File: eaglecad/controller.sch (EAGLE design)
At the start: 110 parts, among them J1 CORTEX_DEBUG_PTH, J2 U.FL, J3 U.FL, J4 U.FL, J6 TSV991ILT, J7 TSV991ILT, U1 AS5047P, U2 TCAN330, U3 LM3671MF-3.3, U6 STM32F042K6, X1 16MHZ-2.5x2mm

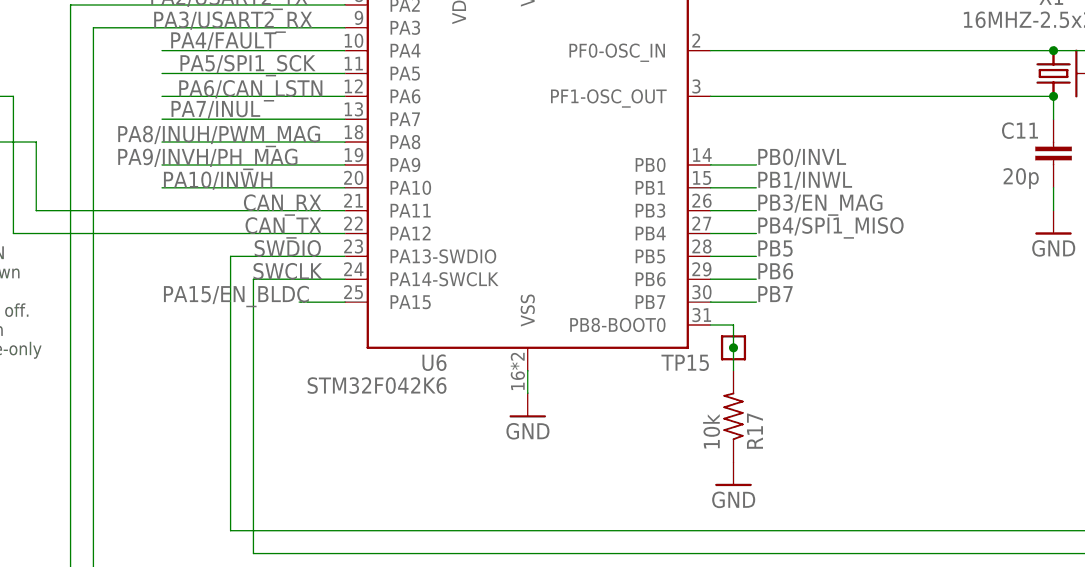
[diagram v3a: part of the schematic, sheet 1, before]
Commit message: Connected the CSn pin of the encoder.
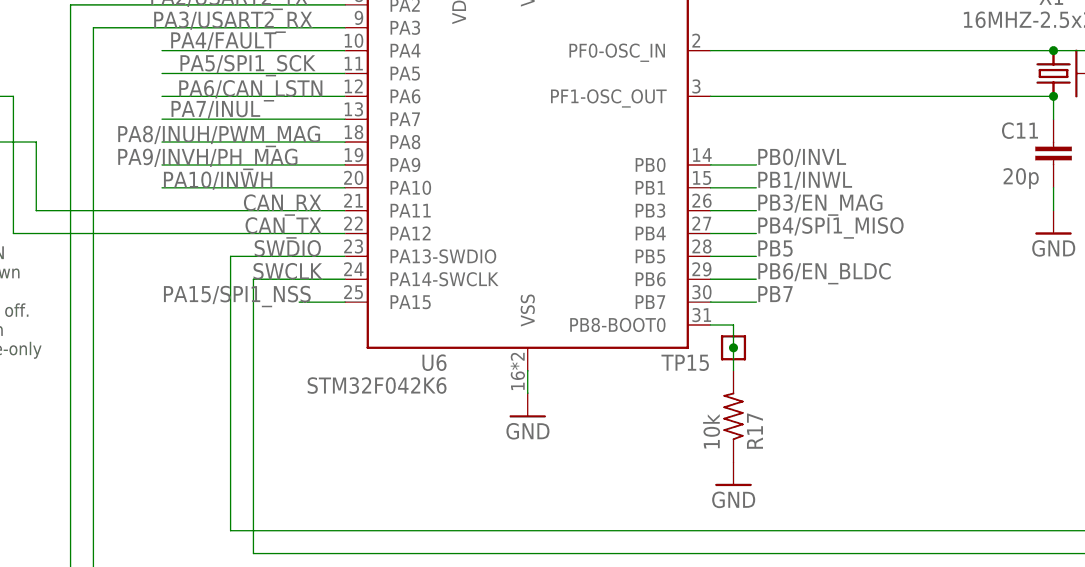
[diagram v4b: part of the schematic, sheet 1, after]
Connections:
- removed net N$9: U1.CSN
- removed net PA15/EN_BLDC: R_EN.2, U6.PA15
- removed net PB6: U6.PB6
- new net PA15/SPI1_NSS: U1.CSN, U6.PA15
- new net PB6/EN_BLDC: R_EN.2, U6.PB6
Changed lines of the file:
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@@
-</segment>
-</net>
-<net name="PA15/EN_BLDC" class="0">
-<segment>
-<pinref part="U6" gate="G$1" pin="PA15"/>
-<wire x1="248.92" y1="114.3" x2="243.84" y2="114.3" width="0.1524" layer="91"/>
-<label x="228.6" y="114.3" size="1.778" layer="95"/>
 </segment>
 </net>
@@
 </segment>
 </net>
-<net name="PB6" class="0">
+<net name="PB6/EN_BLDC" class="0">
 <segment>
 <pinref part="U6" gate="G$1" pin="PB6"/>
@@
 <label x="223.52" y="129.54" size="1.778" layer="95"/>
 <wire x1="248.92" y1="129.54" x2="228.6" y2="129.54" width="0.1524" layer="91"/>
+</segment>
+</net>
+<net name="PA15/SPI1_NSS" class="0">
+<segment>
+<pinref part="U6" gate="G$1" pin="PA15"/>
+<wire x1="248.92" y1="114.3" x2="243.84" y2="114.3" width="0.1524" layer="91"/>
+<label x="228.6" y="114.3" size="1.778" layer="95"/>
 </segment>
 </net>
@@
 </segment>
 </net>
-<net name="PA15/EN_BLDC" class="0">
+<net name="PB6/EN_BLDC" class="0">
 <segment>
 <pinref part="R_EN" gate="G$1" pin="2"/>
@@
 </segment>
 </net>
-<net name="N$9" class="0">
+<net name="PA15/SPI1_NSS" class="0">
 <segment>
 <pinref part="U1" gate="G$1" pin="CSN"/>
 <wire x1="195.58" y1="165.1" x2="185.42" y2="165.1" width="0.1524" layer="91"/>
-</segment>
-</net>
+<label x="172.72" y="165.1" size="1.778" layer="95"/>
+</segment>
+</net>

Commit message: Design review with Nathan. Lots of little changes, mostly cosmetic. Moved from Protocard to smaller ACS board by removing protocard junk.
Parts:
- removed CF1, CF2, CF3: CON-MMCX-F-MOLEX-0734151001, oresat-eagle:CON-MMCX-F-MOLEX-0734151001
- removed CM1: CON-HARTING-FLEX-M-RA-1.27-1515040X601XXX, oresat-eagle:CON-HARTING-FLEX-M-RA-1.27-1515040X601XXX
- removed D3: GREEN, SparkFun-LED:LED-GREEN0603
- removed D4, D5: (no value), adafruit:DIODESMA
- removed J2, J3, J4: U.FL, SparkFun-Connectors:U.FL2PIN
- removed JP2: (no value), pinhead:PINHD-1X12
- removed JP3: (no value), pinhead:PINHD-1X20
- removed JP5, JP6, JP7: (no value), pinhead:PINHD-1X5
- removed R3: 2.7k, rcl_custom:R-US_0402-B-NOSILK
- DRIVER2: device STSPIN250:STSPIN250 -> U-ST-STSPIN250-Brushed-DC-controller:STSPIN250
- JP1: device pinhead:PINHD-2X20 -> pinhead:PINHD-1X4
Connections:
- removed net !SHUTDOWN: CM1.7, CM1.8, JP1.5
- removed net !SHUTDOWN_PH: JP1.6, JP3.3
- removed net CAN_H: CM1.3, CM1.4, JP1.3
- removed net CAN_L: CM1.1, CM1.2, JP1.1
- removed net EN/FAULT: C_EN.1, D4.A, DRIVER1.EN/FAULT, R_EN.1
- removed net N$1: D3.A, R3.1
- removed net N$2: CF2.CENTER, J3.SIGNAL
- removed net N$299: CF1.CENTER, J2.SIGNAL
- removed net N$300: CF3.CENTER, J4.SIGNAL
- removed net SPARE1: CM1.17, CM1.18, JP1.17
- removed net SPARE10: CM1.35, CM1.36, JP1.35
- removed net SPARE10_PH: JP1.36, JP2.10, JP3.18
- removed net SPARE11: CM1.37, CM1.38, JP1.37
- removed net SPARE11_PH: JP1.38, JP2.11, JP3.19
- removed net SPARE12: CM1.39, CM1.40, JP1.39
- removed net SPARE12_PH: JP1.40, JP2.12, JP3.20
- removed net SPARE1_PH: JP1.18, JP2.1, JP3.9
- removed net SPARE2: CM1.19, CM1.20, JP1.19
- removed net SPARE2_PH: JP1.20, JP2.2, JP3.10
- removed net SPARE3: CM1.21, CM1.22, JP1.21
- removed net SPARE3_PH: JP1.22, JP2.3, JP3.11
- removed net SPARE4: CM1.23, CM1.24, JP1.23
- removed net SPARE4_PH: JP1.24, JP2.4, JP3.12
- removed net SPARE5: CM1.25, CM1.26, JP1.25
- removed net SPARE5_PH: JP1.26, JP2.5, JP3.13
- removed net SPARE6: CM1.27, CM1.28, JP1.27
- removed net SPARE6_PH: JP1.28, JP2.6, JP3.14
- removed net SPARE7: CM1.29, CM1.30, JP1.29
- removed net SPARE7_PH: JP1.30, JP2.7, JP3.15
- removed net SPARE8: CM1.31, CM1.32, JP1.31
- removed net SPARE8_PH: JP1.32, JP2.8, JP3.16
- removed net SPARE9: CM1.33, CM1.34, JP1.33
- removed net SPARE9_PH: JP1.34, JP2.9, JP3.17
- removed net VBATT: CM1.13, CM1.14, CM1.15, CM1.16, JP1.7, JP1.9
- net 3.3V: no longer JP3.4, JP5.1, JP5.2, JP5.3, JP5.4, JP5.5, JP6.1, JP6.2, JP6.3, JP6.4, JP6.5
- net CANH_PH: now also JP1.2; no longer JP1.4, JP3.2
- net CAN_L_PH: now also JP1.1; no longer JP1.2, JP3.1
- net FAULT_MAG: no longer D5.A
- net GND: now also JP1.4; no longer CF1.SHIELD, CF2.SHIELD, CF3.SHIELD, CM1.10, CM1.11, CM1.12, CM1.5, CM1.6, CM1.9, D3.C, J2.GND, J3.GND, J4.GND, JP1.12, JP1.14, JP1.16, JP3.6, JP3.7, JP3.8
- net PA0/CURR_FDB_BLDC: no longer R3.2
- net PA4/FAULT: now also C_EN.1, DRIVER1.EN/FAULT, R_EN.1; no longer D4.C, D5.C
- net V_BATT: now also JP1.3; no longer JP1.10, JP1.8, JP3.5, JP7.1, JP7.2, JP7.3, JP7.4, JP7.5
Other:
- note added: "ADD RESISTOR!"
- note added: "BYPASS CAP"
- note added: "CONNECTOR TO ORESAT CARD"
- note added: "FIXME"
- note removed: "What do we connect the CSn pin to? This is for SPI chip select."
- moved on the sheet: C11, C16, C17, C19, C20, C21, C22, C23, C24, C3, C9, D1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

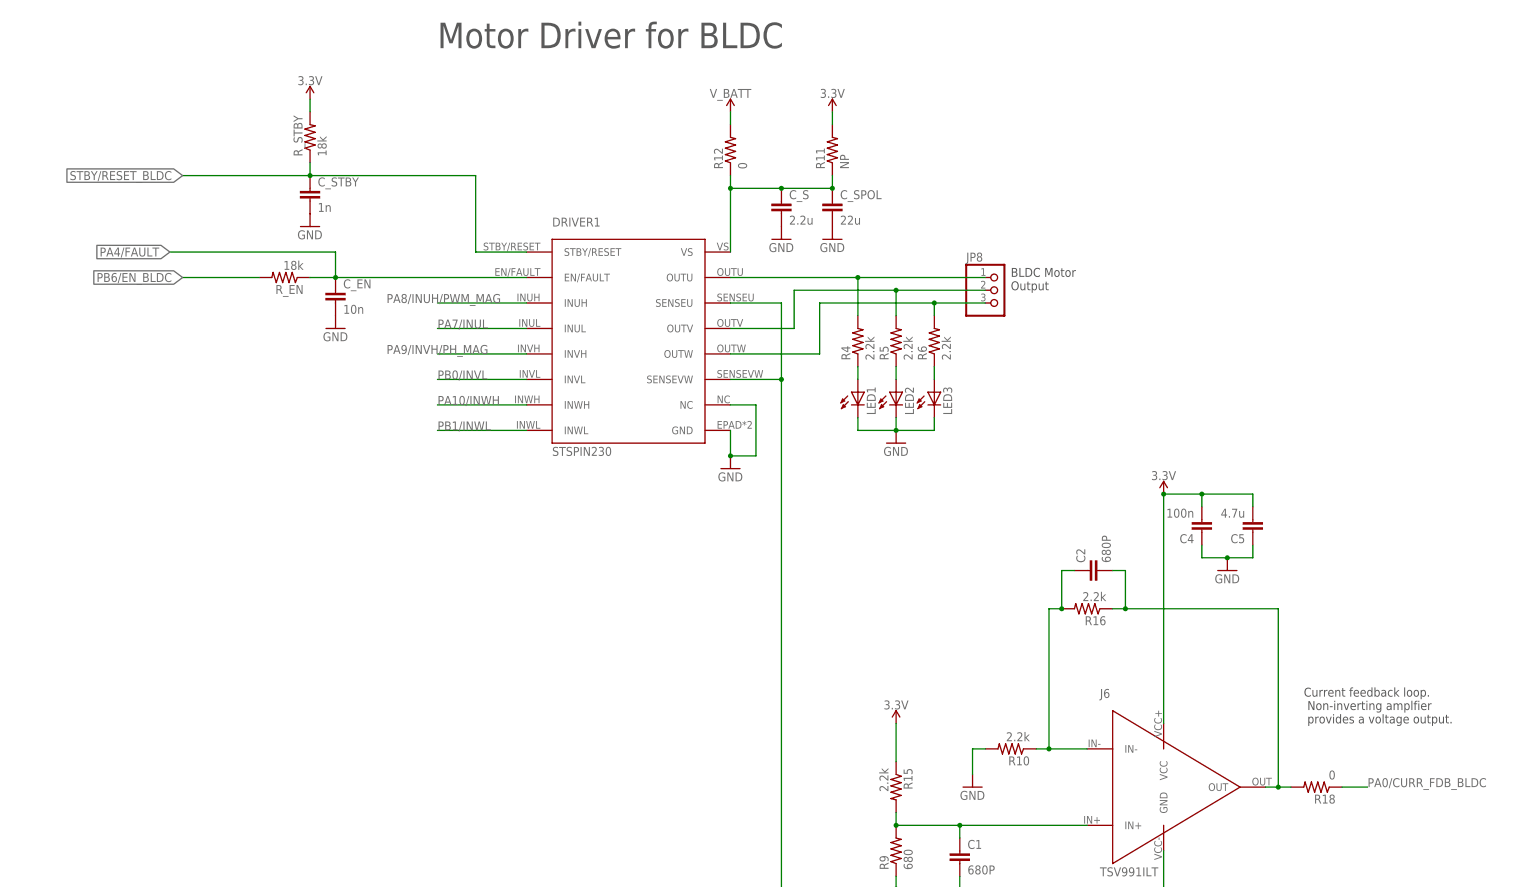
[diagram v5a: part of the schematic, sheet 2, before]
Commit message: Cosmetic fixes: Added labels. All resistors and capacitors are numbered. Updated the symbol of the encoder. Updated the symbol and package of the STSPIN230. Boxed LEDs and placed a note "NP FOR FLIGHT". Other small fixes...
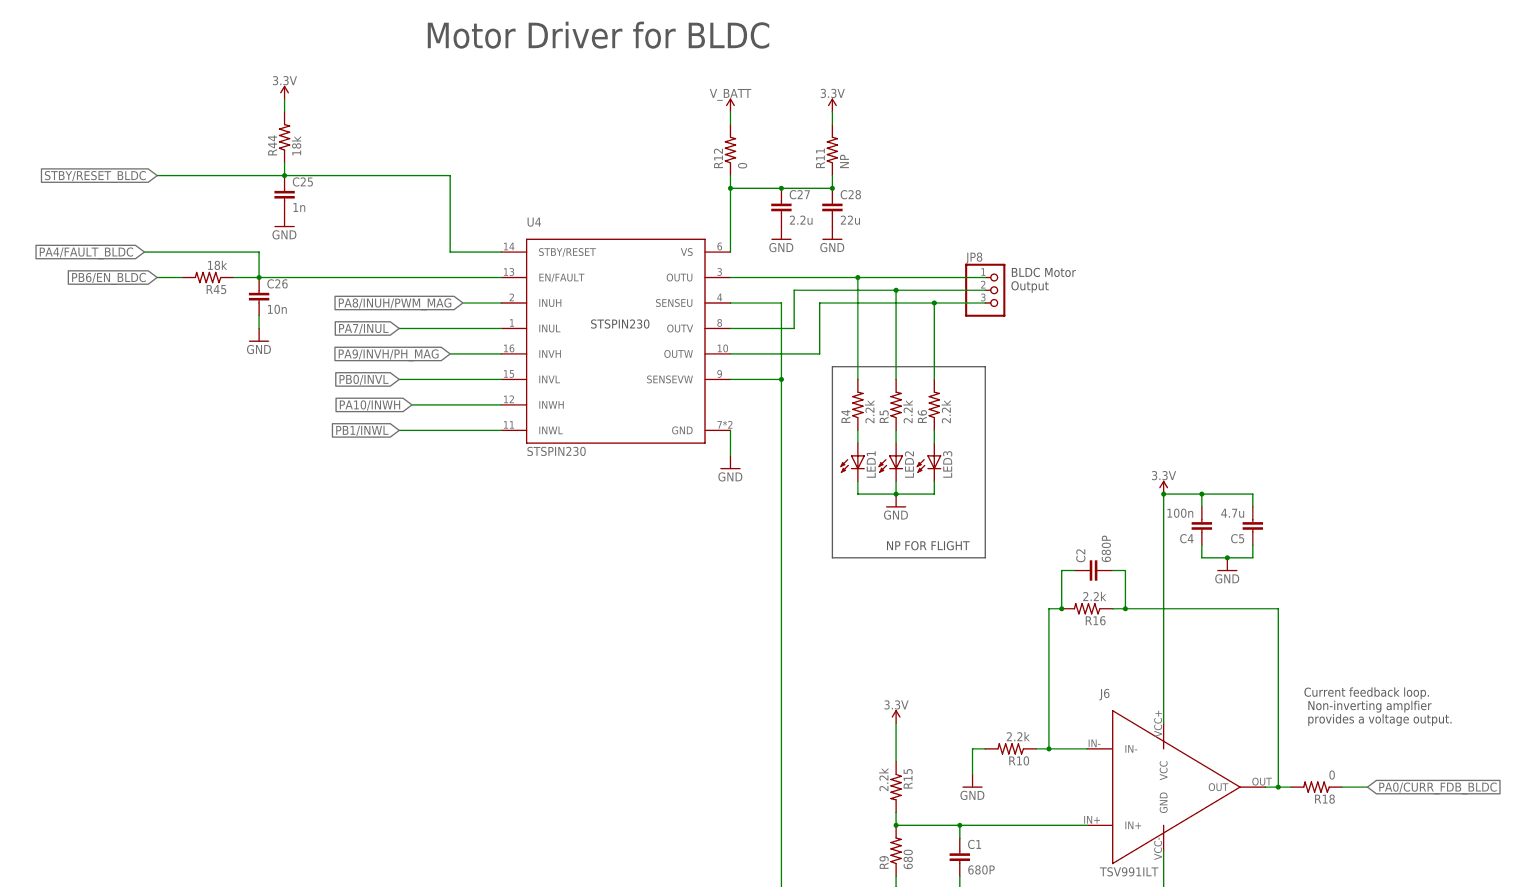
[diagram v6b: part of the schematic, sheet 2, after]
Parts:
- removed C_EN: 10n, rcl:C-EUC0402
- removed C_STBY: 1n, rcl:C-EUC0402
- removed DRIVER1: STSPIN230, STSPIN230:STSPIN230
- removed R_EN, R_STBY: 18k, rcl:R-US_R0402
- added C25: 1n, rcl:C-EUC0402
- added C26: 10n, rcl:C-EUC0402
- added C33: 2.2n, rcl:C-EUC0402
- added R3: 10k, rcl:R-US_R0402
- added R44, R45: 18k, rcl:R-US_R0402
- added U4: STSPIN230, U-ST-STSPIN230-BLDC-controller:STSPIN230
- C6: value 2.2n -> 100n
- U1: device AS5047P:AS5047P -> U-AMS-AS5047P-encoder:AS5047P
- renumbered C_EN1 to C30, C_OFF to C34, C_S to C27, C_S1 to C31, C_SPOL to C28, C_SPOL1 to C32, C_STBY1 to C29, RC_OFF to R48, R_EN1 to R47, R_OFF to R49, R_STBY1 to R46
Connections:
- removed net FAULT_MAG: C30.1, DRIVER2.EN/FAULT, R47.1
- removed net N$21: DRIVER1.OUTW, JP8.3, R6.2
- removed net N$7: DRIVER1.OUTU, JP8.1, R4.2
- removed net N$8: DRIVER1.OUTV, JP8.2, R5.2
- removed net PA4/FAULT: C_EN.1, DRIVER1.EN/FAULT, R_EN.1, U6.PA4
- removed net PB7: U6.PB7
- new net N$1: R3.2
- new net PA4/FAULT_BLDC: C26.1, R45.1, U4.EN/FAULT, U6.PA4
- new net PB7/FAULT_MAG: C30.1, DRIVER2.EN/FAULT, R47.1, U6.PB7
- new net U: JP8.1, R4.2, U4.OUTU
- new net V: JP8.2, R5.2, U4.OUTV
- new net W: JP8.3, R6.2, U4.OUTW
- net 3.3V: now also C6.1, R3.1, R44.2; no longer R_STBY.2, U1.MOSI
- net GND: now also C25.2, C26.2, C33.1, C6.2, U1.TEST, U4.GND; no longer C6.1, C_EN.2, C_STBY.2, DRIVER1.GND, DRIVER1.NC
- net N$12: now also U4.VS; no longer DRIVER1.VS
- net N$13: now also U4.SENSEU, U4.SENSEVW; no longer DRIVER1.SENSEU, DRIVER1.SENSEVW
- net N$25: now also C33.2; no longer C6.2
- net PA10/INWH: now also U4.INWH; no longer DRIVER1.INWH
- net PA15/SPI1_NSS: no longer U1.CSN
- net PA5/SPI1_SCK: no longer U1.CLK
- net PA7/INUL: now also U4.INUL; no longer DRIVER1.INUL
- net PA8/INUH/PWM_MAG: now also U4.INUH; no longer DRIVER1.INUH
- net PA9/INVH/PH_MAG: now also U4.INVH; no longer DRIVER1.INVH
- net PB0/INVL: now also U4.INVL; no longer DRIVER1.INVL
- net PB1/INWL: now also U4.INWL; no longer DRIVER1.INWL
- net PB4/SPI1_MISO: no longer U1.MISO
- net PB6/EN_BLDC: now also R45.2; no longer R_EN.2
- net STBY/RESET_BLDC: now also C25.1, R44.1, U4.STBY/RESET; no longer C_STBY.1, DRIVER1.STBY/RESET, R_STBY.1
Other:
- note added: "NP FOR FLIGHT"
- note removed: "ADD RESISTOR!"
- note removed: "BYPASS CAP"
- note removed: "FIXME"
- moved on the sheet: C17, LED1, LED2, LED3, LED4, LED5, R21, R22, R23, R24, R25, R26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

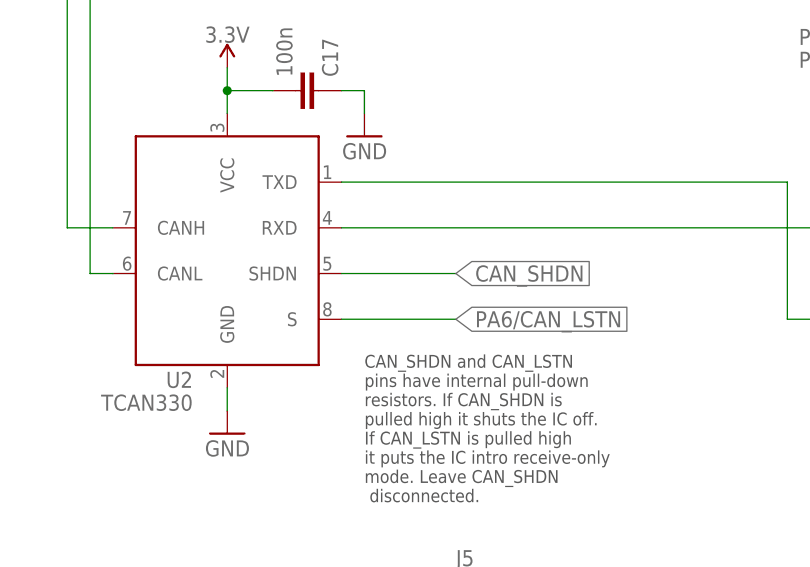
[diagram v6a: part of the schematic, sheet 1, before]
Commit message: Added a testpoint to the CAN transciever.
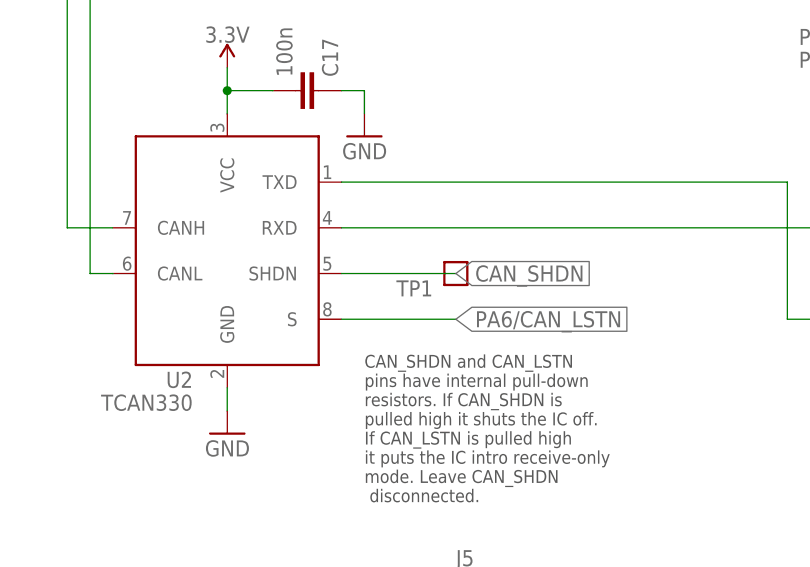
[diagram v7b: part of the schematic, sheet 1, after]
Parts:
- added TP1: TEST-POINT, Tova:TEST-POINT
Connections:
- net CAN_SHDN: now also TP1.1
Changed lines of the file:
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@@
 <part name="GND2" library="supply1" library_urn="urn:adsk.eagle:library:371" deviceset="GND" device=""/>
 <part name="U4" library="U-ST-STSPIN230-BLDC-controller" deviceset="STSPIN230" device=""/>
+<part name="TP1" library="Tova" deviceset="TEST-POINT" device=""/>
 </parts>
 <sheets>
@@
 <instance part="SUPPLY2" gate="G$1" x="68.58" y="187.96"/>
 <instance part="GND3" gate="1" x="68.58" y="167.64" rot="MR0"/>
+<instance part="TP1" gate="G$1" x="129.54" y="124.46" smashed="yes" rot="MR0">
+<attribute name="NAME" x="127" y="121.92" size="1.778" layer="95" font="vector" rot="MR0"/>
+</instance>
 </instances>
 <busses>
@@
 <pinref part="U2" gate="G$1" pin="SHDN"/>
 <label x="129.54" y="124.46" size="1.778" layer="95" xref="yes"/>
-<wire x1="116.84" y1="124.46" x2="129.54" y2="124.46" width="0.1524" layer="91"/>
-</segment>
-</net>
+<pinref part="TP1" gate="G$1" pin="1"/>
+<wire x1="129.54" y1="124.46" x2="116.84" y2="124.46" width="0.1524" layer="91"/>
+</segment>
+</net>

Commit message: Nice job, Nathan! Did a bit of visual polish, updated AMS symbol to be more compact. Big changes: Added new TPS63070 SPS circuit from solar board, redid LEDs on magnetorquer. BLDC LEDs should be that way too, but no reason to have 6 LEDs...
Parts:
- removed C19, C23, C24: 100n, rcl_custom:C-EU0402-B-NOSILK
- removed C20, C21: 4.7u, rcl:C-EUC0603
- removed J6, J7: TSV991ILT, TSV991ILT:TSV991ILT
- removed JP9: (no value), adafruit:PINHD-1X3
- removed L1: 10u, rcl:L-USL2012C
- removed R13: 665k, rcl_custom:R-US_0402-B-NOSILK
- removed R14: 332k, rcl_custom:R-US_0402-B-NOSILK
- removed U3: LM3671MF-3.3, LM3761:LM3761
- added C13: 10u, oresat-rcl:C-EU0603-B-NOSILK
- added C14: 100n, rcl_custom:C-EU0402-B-NOSILK
- added C15, C18: 10u, oresat-rcl:C-EU0805-B-NOSILK
- added C35: 22u, oresat-rcl:C-EU0603-B-NOSILK
- added C36, C37: 22u, oresat-rcl:C-EU0805-B-NOSILK
- added JP2: (no value), pinhead:PINHD-1X2
- added L2: 1.5 uH, L-Coilcraft-XFL4020:L-COILCRAFT-XFL4020
- added R34, R38: 10k, rcl_custom:R-US_0402-B-NOSILK
- added R35: 0, rcl_custom:R-US_0805-B-NOSILK
- added R36: 470k, rcl_custom:R-US_0402-B-NOSILK
- added R37: 100k, rcl_custom:R-US_0402-B-NOSILK
- added R39, R40: NP, rcl_custom:R-US_0402-B-NOSILK
- added TP26, TP27, TP28, TP29, TP6: TEST-POINT, Tova:TEST-POINT
- added U10: TPS63070, ic-pwr-tps63070x:TPS63070X
- added U5, U7: TSV991ILT, TSV991ILT:TSV991ILT
- C1: value 680P -> 680p
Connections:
- net CANH_PH renamed CAN_H
- net PA9/INVH/PH_MAG renamed PA9/INVH/DIR_MAG
- removed net CAN_L_PH: JP1.1, U2.CANL
- removed net STEPD: L1.2, U3.SW
- removed net VDIV: C24.1, R13.1, R14.2, U3.EN
- new net CAN_L: JP1.3, U2.CANL
- new net TPS-EN: R34.1, R40.2, TP29.1, U10.EN, U10.PS/SYNC
- new net TPS-FB: R36.1, R37.2, U10.FB
- new net TPS-FB2: TP27.1, U10.FB2
- new net TPS-L1: L2.1, U10.L1
- new net TPS-L2: L2.2, U10.L2
- new net TPS-PG: R39.1, TP26.1, U10.PG
- new net TPS-VAUX: C14.1, U10.VAUX
- new net TPS-VIN: C13.1, C15.1, C18.1, R34.2, R35.1, U10.VIN
- new net TPS-VSEL: R38.2, TP28.1, U10.VSEL
- net 3.3V: now also C35.1, C36.1, C37.1, R36.2, R39.2, TP6.1, U10.VOUT, U5.VCC, U7.VCC; no longer C19.1, C21.1, J6.VCC, J7.VCC, L1.1, U3.FB
- net GND: now also C13.2, C14.2, C15.2, C18.2, C35.2, C36.2, C37.2, R37.1, R38.1, R40.1, U10.GND, U10.PGND, U5.GND, U7.GND; no longer C19.2, C20.2, C21.2, C23.2, C24.2, J6.GND, J7.GND, LED4.C, LED5.C, R14.1, U3.GND
- net N$1: now also U1.MOSI
- net N$14: now also U5.IN-; no longer J6.IN-
- net N$15: now also U7.IN+; no longer J7.IN+
- net N$16: now also U5.IN+; no longer J6.IN+
- net N$17: now also U7.IN-; no longer J7.IN-
- net N$24: now also JP2.1, LED5.C; no longer JP9.1
- net N$26: now also JP2.2, LED4.C; no longer JP9.3
- net N$27: now also U7.OUT; no longer J7.OUT
- net N$29: now also U5.OUT; no longer J6.OUT
- net PA15/SPI1_NSS: now also U1.CSN
- net PA5/SPI1_SCK: now also U1.SCLK
- net PB4/SPI1_MISO: now also U1.MISO
- net V_BATT: now also JP1.1, R35.2; no longer C20.1, C23.1, JP1.3, R13.2, U3.VIN
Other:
- note added: "0805"
- note added: "3.3V SPS"
- note added: "BLDC ENCODER"
- note added: "BLDC Motor Driver"
- note added: "Correct command is FF!"
- note added: "Current feedback to STM32."
- note added: "In case we need to switch mag to a regulated supply"
- note added: "In case we need to switch motor to a regulated supply"
- note added: "Magnetorquer Driver"
- note added: "NP for Flight"
- note added: "STM32 Control"
- note added: "STM32 Current Feedback"
- note added: "STM32 PWM"
- note added: "STM32 SPI"
- note added: "TBD: CONNECTOR TO ORESAT ACS CARD"
- note added: "TO BLDC MOTOR"
- note added: "TO MAGNETORQUER"
- note removed: "BLDC Motor Output"
- note removed: "CONNECTOR TO ORESAT CARD"
- note removed: "Current feedback loop. Non-inverting amplfier provides a voltage output."
- note removed: "Encoder"
- note removed: "Magnetorquer Output"
- note removed: "Motor Driver for BLDC"
- note removed: "Motor Driver for Magnetorquer"
- note removed: "Turn on when EN > 1; with 1/3 divier, that's approximately 3.0V."
